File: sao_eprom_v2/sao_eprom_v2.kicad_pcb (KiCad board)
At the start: 4 copper layers, 62 parts, among them J1 Conn_01x03, J2 USB_C_Receptacle_USB2.0, J3 Conn_02x03_Odd_Even, Q1 RE1C002UNTCL, Q2 RE1C002ZPTL, Q3 RE1C002UNTCL, Q4 RE1C002ZPTL, Q5 RE1C002UNTCL, Q6 RE1C002ZPTL, U1 W25Q128JVS, U10 AP3012, U2 RP2040, U3 24LC00, U4 74HC273, U5 multi_eprom, U6 74LVC4245A-Q100, U7 74HC273, U8 SY8079AAC, U9 AP3012, X1 YSO110TR

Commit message: the experiment
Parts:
- added C14: 100n, Capacitor_SMD:C_0402_1005Metric_Pad0.74x0.62mm_HandSolder, F.Cu at (167.7, 90.5)
- added C15: 100n, Capacitor_SMD:C_0402_1005Metric_Pad0.74x0.62mm_HandSolder, F.Cu at (155.0, 85.0)
- added C16: 100n, Capacitor_SMD:C_0402_1005Metric_Pad0.74x0.62mm_HandSolder, F.Cu at (129.4, 69.5)
- added C17: 100n, Capacitor_SMD:C_0402_1005Metric_Pad0.74x0.62mm_HandSolder, F.Cu at (129.4, 71.8)
- added C18: 100n, Capacitor_SMD:C_0402_1005Metric_Pad0.74x0.62mm_HandSolder, F.Cu at (138.6, 64.5)
- added C19: 100n, Capacitor_SMD:C_0402_1005Metric_Pad0.74x0.62mm_HandSolder, F.Cu at (148.1, 71.6)
- added C20: 100n, Capacitor_SMD:C_0402_1005Metric_Pad0.74x0.62mm_HandSolder, F.Cu at (144.5, 71.6)
- added C21: 100n, Capacitor_SMD:C_0402_1005Metric_Pad0.74x0.62mm_HandSolder, F.Cu at (152.5, 63.0)
- added C22: 100n, Capacitor_SMD:C_0402_1005Metric_Pad0.74x0.62mm_HandSolder, F.Cu at (138.6, 65.5)
- C1, C2, C3, C4, C5, C6: footprint Capacitor_SMD:C_0402_1005Metric -> Capacitor_SMD:C_0402_1005Metric_Pad0.74x0.62mm_HandSolder
- C10, C11, C8, C9: footprint Capacitor_SMD:C_0603_1608Metric -> Capacitor_SMD:C_0603_1608Metric_Pad1.08x0.95mm_HandSolder
- C12, C13, C7: footprint Capacitor_SMD:C_0805_2012Metric -> Capacitor_SMD:C_0805_2012Metric_Pad1.18x1.45mm_HandSolder
- J3: value Conn_02x03_Odd_Even -> sao_v2_addon_tht; footprint Connector_PinHeader_2.54mm:PinHeader_2x03_P2.54mm_Vertical -> simple_add_on_v2:sao_v2_addon_tht
- U4, U7: value 74HC273 -> 74LS573
- moved U3 100.6 mm to (169.7, 94.0)
- moved U1 91.9 mm to (162.5, 83.0)
- moved R9 88.1 mm to (152.5, 66.0), turned to 180 degrees
- moved R8 87.9 mm to (152.5, 67.0), turned to 180 degrees
- moved C2 69.9 mm to (152.5, 65.0), turned to 180 degrees
- moved C4 69.9 mm to (152.5, 69.0), turned to 180 degrees
- moved C1 69.8 mm to (152.5, 64.0), turned to 180 degrees
- moved C3 69.8 mm to (152.5, 68.0), turned to 180 degrees
- moved U2 62.9 mm to (145.5, 64.2), turned to -90 degrees
- moved J3 53.3 mm to (109.8, 71.5)
- moved J2 37.9 mm to (106.0, 45.0), turned to -90 degrees
- moved C13 37.0 mm to (117.0, 41.5), turned to 90 degrees
- moved C12 33.5 mm to (115.0, 41.5), turned to 90 degrees
- moved C5 31.9 mm to (121.2, 40.7), turned to 90 degrees
- moved D4 31.8 mm to (118.5, 50.2), turned to 180 degrees
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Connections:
- net Net-(U2-VREG_VOUT) renamed +1V1
- net Net-(U5-D0) renamed /EPROM and level shifters/D0H
- net Net-(U5-D1) renamed /EPROM and level shifters/D1H
- net Net-(U5-D2) renamed /EPROM and level shifters/D2H
- net Net-(U5-D3) renamed /EPROM and level shifters/D3H
- net Net-(U5-D4) renamed /EPROM and level shifters/D4H
- net Net-(U5-D5) renamed /EPROM and level shifters/D5H
- net Net-(U5-D6) renamed /EPROM and level shifters/D6H
- net Net-(U5-D7) renamed /EPROM and level shifters/D7H
- C10 pad 2: +3.3V -> +3V3
- C8 pad 2: +3.3V -> +3V3
- D1 pad 1: /EPROM and level shifters/Vdet -> /EPROM and level shifters/Q15
- D2 pad 1: /EPROM and level shifters/VppA -> /EPROM and level shifters/VppB
- D2 pad 2: Net-(D2-A) -> /EPROM and level shifters/~{OE}
- D3 pad 1: /EPROM and level shifters/VppB -> /EPROM and level shifters/Q9
- D3 pad 2: /EPROM and level shifters/~{OE} -> Net-(D3-A)
- J2 pad B8: SBU1 -> SBU2
- J3 pad 1: GND -> +3V3
- J3 pad 2: +3V3 -> GND
- J3 pad 3: SCL -> SDA
- J3 pad 4: SDA -> SCL
- L2 pad 1: +3.3V -> +3V3
- L3 pad 1: +3.3V -> +3V3
- Q2 pad 3: /EPROM and level shifters/VppA -> /EPROM and level shifters/Q15
- Q6 pad 3: /EPROM and level shifters/Vdet -> /EPROM and level shifters/Q9
- U10 pad 5: +3.3V -> +3V3
- U2 pad 40: unconnected-(U2-GPIO28_ADC2-Pad40) -> SBU1
- U2 pad 41: unconnected-(U2-GPIO29_ADC3-Pad41) -> SBU2
- U4 pad 1: +3V3 -> GND
- U4 pad 12: Net-(U4-Q4) -> /EPROM and level shifters/Q7
- U4 pad 13: /EPROM and level shifters/A4 -> /EPROM and level shifters/Q6
- U4 pad 14: /EPROM and level shifters/A5 -> /EPROM and level shifters/Q5
- U4 pad 15: Net-(U4-Q5) -> /EPROM and level shifters/Q4
- U4 pad 16: Net-(U4-Q6) -> /EPROM and level shifters/Q3
- U4 pad 17: /EPROM and level shifters/A6 -> /EPROM and level shifters/Q2
- U4 pad 18: /EPROM and level shifters/A7 -> /EPROM and level shifters/Q1
- U4 pad 19: Net-(U4-Q7) -> /EPROM and level shifters/Q0
- U4 pad 2: Net-(U4-Q0) -> /EPROM and level shifters/A0
- U4 pad 3: /EPROM and level shifters/A0 -> /EPROM and level shifters/A1
- U4 pad 4: /EPROM and level shifters/A1 -> /EPROM and level shifters/A2
- U4 pad 5: Net-(U4-Q1) -> /EPROM and level shifters/A3
- U4 pad 6: Net-(U4-Q2) -> /EPROM and level shifters/A4
- U4 pad 7: /EPROM and level shifters/A2 -> /EPROM and level shifters/A5
- U4 pad 8: /EPROM and level shifters/A3 -> /EPROM and level shifters/A6
- U4 pad 9: Net-(U4-Q3) -> /EPROM and level shifters/A7
- U5 pad 1: /EPROM and level shifters/VppA -> /EPROM and level shifters/Q15
- U5 pad 10: Net-(U4-Q0) -> /EPROM and level shifters/Q0
- U5 pad 2: Net-(U5-A12) -> /EPROM and level shifters/Q12
- U5 pad 21: Net-(U5-A10) -> /EPROM and level shifters/Q10
- U5 pad 23: Net-(U5-A11) -> /EPROM and level shifters/Q11
- U5 pad 24: /EPROM and level shifters/Vdet -> /EPROM and level shifters/Q9
- U5 pad 25: Net-(U5-A8) -> /EPROM and level shifters/Q8
- U5 pad 26: Net-(U5-A13) -> /EPROM and level shifters/Q13
- U5 pad 27: Net-(U5-A14) -> /EPROM and level shifters/Q14
- U5 pad 3: Net-(U4-Q7) -> /EPROM and level shifters/Q7
- U5 pad 4: Net-(U4-Q6) -> /EPROM and level shifters/Q6
- U5 pad 5: Net-(U4-Q5) -> /EPROM and level shifters/Q5
- U5 pad 6: Net-(U4-Q4) -> /EPROM and level shifters/Q4
- U5 pad 7: Net-(U4-Q3) -> /EPROM and level shifters/Q3
- U5 pad 8: Net-(U4-Q2) -> /EPROM and level shifters/Q2
- U5 pad 9: Net-(U4-Q1) -> /EPROM and level shifters/Q1
- U7 pad 1: +3V3 -> GND
- U7 pad 12: Net-(U5-A12) -> Net-(D1-A)
- U7 pad 13: /EPROM and level shifters/A4 -> /EPROM and level shifters/Q14
- U7 pad 14: /EPROM and level shifters/A5 -> /EPROM and level shifters/Q13
- U7 pad 15: Net-(U5-A13) -> /EPROM and level shifters/Q12
- U7 pad 16: Net-(U5-A14) -> /EPROM and level shifters/Q11
- U7 pad 17: /EPROM and level shifters/A6 -> /EPROM and level shifters/Q10
- U7 pad 18: /EPROM and level shifters/A7 -> Net-(D3-A)
- U7 pad 19: Net-(D2-A) -> /EPROM and level shifters/Q8
- U7 pad 2: Net-(U5-A8) -> /EPROM and level shifters/A0
- U7 pad 3: /EPROM and level shifters/A0 -> /EPROM and level shifters/A1
- U7 pad 4: /EPROM and level shifters/A1 -> /EPROM and level shifters/A2
- U7 pad 5: Net-(D1-A) -> /EPROM and level shifters/A3
- U7 pad 6: Net-(U5-A10) -> /EPROM and level shifters/A4
- U7 pad 7: /EPROM and level shifters/A2 -> /EPROM and level shifters/A5
- U7 pad 8: /EPROM and level shifters/A3 -> /EPROM and level shifters/A6
- U7 pad 9: Net-(U5-A11) -> /EPROM and level shifters/A7
- U9 pad 5: +3.3V -> +3V3
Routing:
- net GND: track 0.00 -> 80.7 mm, vias 0 -> 16
- net +3V3: track 0.00 -> 60.9 mm, vias 0 -> 13
- net /EPROM and level shifters/VppB: track 0.00 -> 60.7 mm, vias 0 -> 2
- net /EPROM and level shifters/Q9: track 0.00 -> 58.6 mm, vias 0 -> 2
- net /EPROM and level shifters/D7H: track 0.00 -> 45.3 mm, vias 0 -> 2
- net /EPROM and level shifters/D3H: track 0.00 -> 44.7 mm, vias 0 -> 2
- net /EPROM and level shifters/D4H: track 0.00 -> 37.7 mm, vias 0 -> 2
- net /EPROM and level shifters/D6H: track 0.00 -> 37.7 mm, vias 0 -> 2
- net /EPROM and level shifters/Q10: track 0.00 -> 37.2 mm, vias 0 -> 1
- net /EPROM and level shifters/D5H: track 0.00 -> 33.4 mm, vias 0 -> 2
- net /EPROM and level shifters/Q11: track 0.00 -> 31.9 mm
- net Net-(D3-A): track 0.00 -> 28.1 mm
- net /EPROM and level shifters/A7: track 0.00 -> 27.5 mm, vias 0 -> 2
- net /EPROM and level shifters/Q8: track 0.00 -> 26.9 mm, vias 0 -> 1
- net /EPROM and level shifters/A6: track 0.00 -> 26.0 mm, vias 0 -> 2
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- added copper zone on F.Cu, net +1V1
- added copper zone on F.Cu, net +3V3

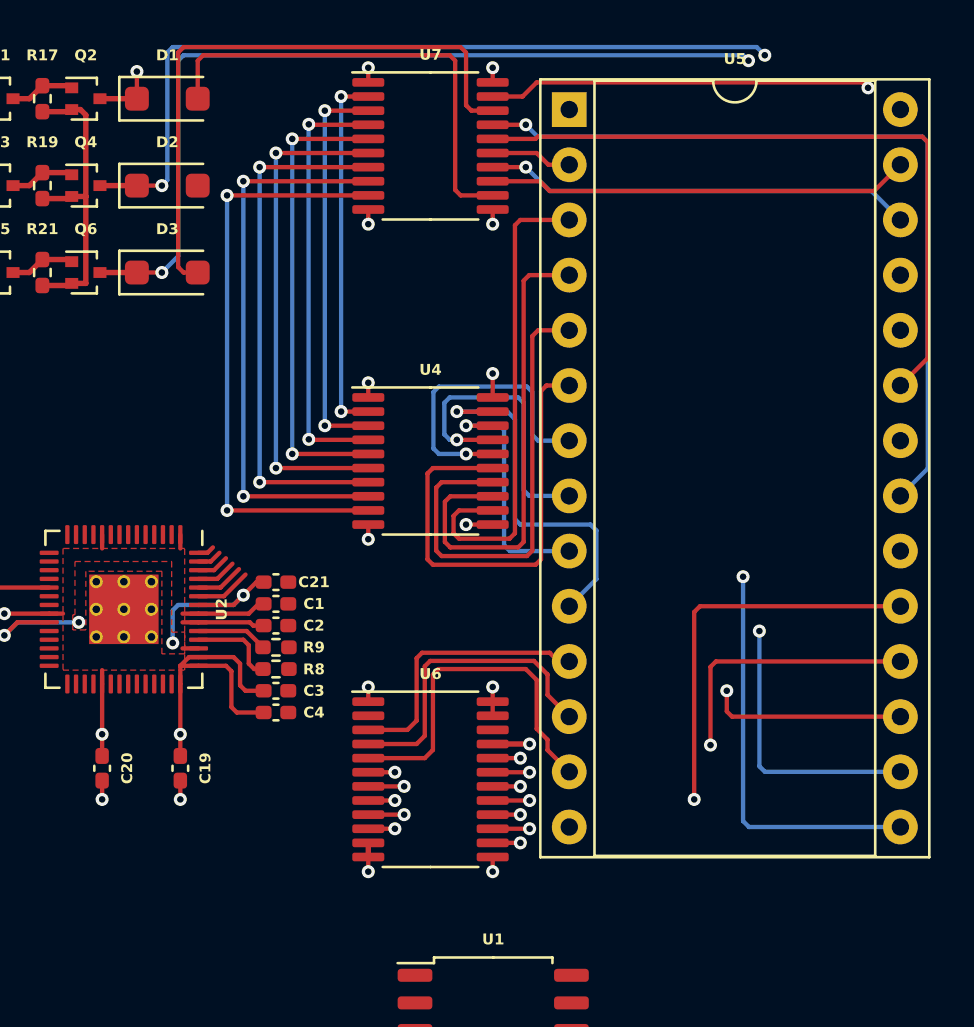
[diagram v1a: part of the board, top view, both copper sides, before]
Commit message: Flip the CHIPS upside down to make routing easier
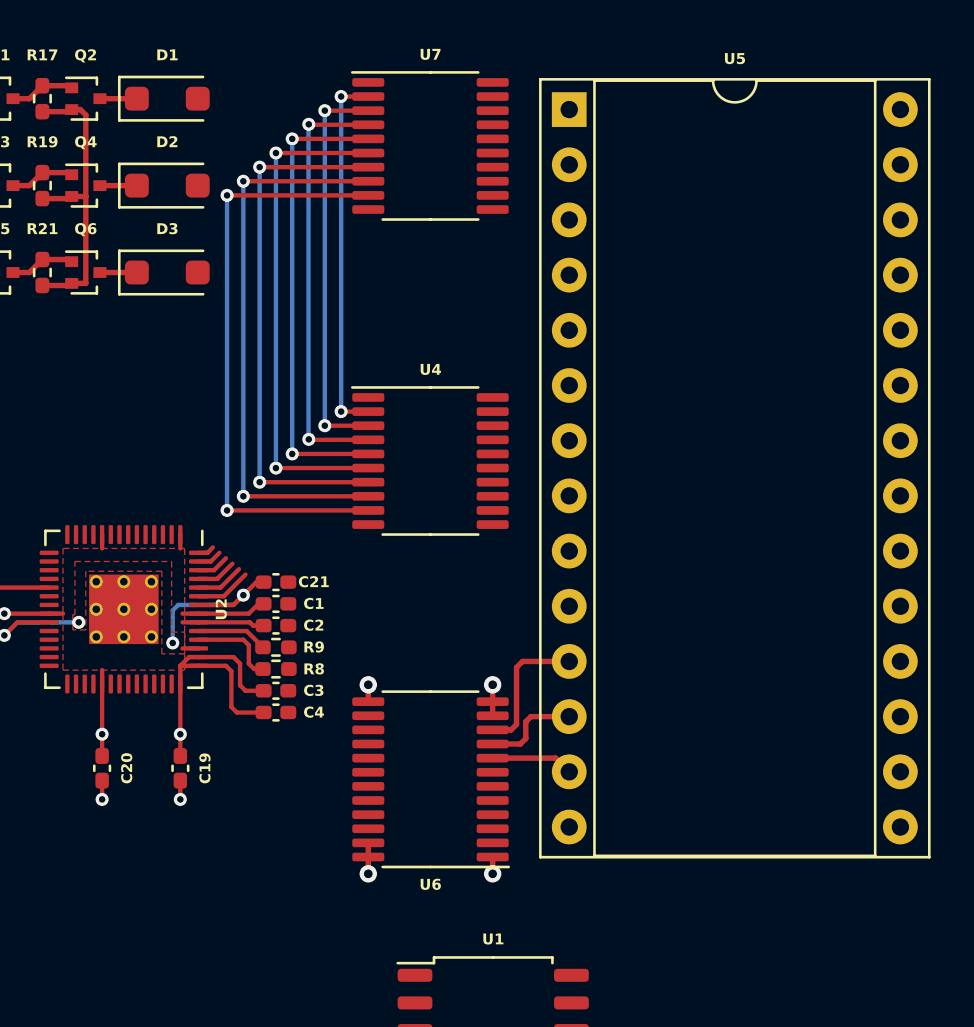
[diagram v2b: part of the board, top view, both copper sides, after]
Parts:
- turned U6 to 180 degrees
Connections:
- U4 pad 12: /EPROM and level shifters/Q7 -> /EPROM and level shifters/Q0
- U4 pad 13: /EPROM and level shifters/Q6 -> /EPROM and level shifters/Q1
- U4 pad 14: /EPROM and level shifters/Q5 -> /EPROM and level shifters/Q2
- U4 pad 15: /EPROM and level shifters/Q4 -> /EPROM and level shifters/Q3
- U4 pad 16: /EPROM and level shifters/Q3 -> /EPROM and level shifters/Q4
- U4 pad 17: /EPROM and level shifters/Q2 -> /EPROM and level shifters/Q5
- U4 pad 18: /EPROM and level shifters/Q1 -> /EPROM and level shifters/Q6
- U4 pad 19: /EPROM and level shifters/Q0 -> /EPROM and level shifters/Q7
- U4 pad 2: /EPROM and level shifters/A0 -> /EPROM and level shifters/A7
- U4 pad 3: /EPROM and level shifters/A1 -> /EPROM and level shifters/A6
- U4 pad 4: /EPROM and level shifters/A2 -> /EPROM and level shifters/A5
- U4 pad 5: /EPROM and level shifters/A3 -> /EPROM and level shifters/A4
- U4 pad 6: /EPROM and level shifters/A4 -> /EPROM and level shifters/A3
- U4 pad 7: /EPROM and level shifters/A5 -> /EPROM and level shifters/A2
- U4 pad 8: /EPROM and level shifters/A6 -> /EPROM and level shifters/A1
- U4 pad 9: /EPROM and level shifters/A7 -> /EPROM and level shifters/A0
- U6 pad 10: /EPROM and level shifters/D7H -> /EPROM and level shifters/D0H
- U6 pad 14: /EPROM and level shifters/D7 -> /EPROM and level shifters/D0
- U6 pad 15: /EPROM and level shifters/D6 -> /EPROM and level shifters/D1
- U6 pad 16: /EPROM and level shifters/D5 -> /EPROM and level shifters/D2
- U6 pad 17: /EPROM and level shifters/D4 -> /EPROM and level shifters/D3
- U6 pad 18: /EPROM and level shifters/D3 -> /EPROM and level shifters/D4
- U6 pad 19: /EPROM and level shifters/D2 -> /EPROM and level shifters/D5
- U6 pad 20: /EPROM and level shifters/D1 -> /EPROM and level shifters/D6
- U6 pad 21: /EPROM and level shifters/D0 -> /EPROM and level shifters/D7
- U6 pad 3: /EPROM and level shifters/D0H -> /EPROM and level shifters/D7H
- U6 pad 4: /EPROM and level shifters/D1H -> /EPROM and level shifters/D6H
- U6 pad 5: /EPROM and level shifters/D2H -> /EPROM and level shifters/D5H
- U6 pad 6: /EPROM and level shifters/D3H -> /EPROM and level shifters/D4H
- U6 pad 7: /EPROM and level shifters/D4H -> /EPROM and level shifters/D3H
- U6 pad 8: /EPROM and level shifters/D5H -> /EPROM and level shifters/D2H
- U6 pad 9: /EPROM and level shifters/D6H -> /EPROM and level shifters/D1H
- U7 pad 12: Net-(D1-A) -> /EPROM and level shifters/Q8
- U7 pad 13: /EPROM and level shifters/Q14 -> Net-(D3-A)
- U7 pad 14: /EPROM and level shifters/Q13 -> /EPROM and level shifters/Q10
- U7 pad 15: /EPROM and level shifters/Q12 -> /EPROM and level shifters/Q11
- U7 pad 16: /EPROM and level shifters/Q11 -> /EPROM and level shifters/Q12
- U7 pad 17: /EPROM and level shifters/Q10 -> /EPROM and level shifters/Q13
- U7 pad 18: Net-(D3-A) -> /EPROM and level shifters/Q14
- U7 pad 19: /EPROM and level shifters/Q8 -> Net-(D1-A)
- U7 pad 2: /EPROM and level shifters/A0 -> /EPROM and level shifters/A7
- U7 pad 3: /EPROM and level shifters/A1 -> /EPROM and level shifters/A6
- U7 pad 4: /EPROM and level shifters/A2 -> /EPROM and level shifters/A5
- U7 pad 5: /EPROM and level shifters/A3 -> /EPROM and level shifters/A4
- U7 pad 6: /EPROM and level shifters/A4 -> /EPROM and level shifters/A3
- U7 pad 7: /EPROM and level shifters/A5 -> /EPROM and level shifters/A2
- U7 pad 8: /EPROM and level shifters/A6 -> /EPROM and level shifters/A1
- U7 pad 9: /EPROM and level shifters/A7 -> /EPROM and level shifters/A0
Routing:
- net /EPROM and level shifters/VppB: track 60.7 -> 1.70 mm, vias 2 -> 0
- net /EPROM and level shifters/Q9: track 58.6 -> 1.70 mm, vias 2 -> 0
- net /EPROM and level shifters/D7H: track 45.3 -> 0.00 mm, vias 2 -> 0
- net /EPROM and level shifters/D3H: track 44.7 -> 0.00 mm, vias 2 -> 0
- net /EPROM and level shifters/D4H: track 37.7 -> 0.00 mm, vias 2 -> 0
- net /EPROM and level shifters/D6H: track 37.7 -> 0.00 mm, vias 2 -> 0
- net /EPROM and level shifters/Q10: track 37.2 -> 0.00 mm, vias 1 -> 0
- net /EPROM and level shifters/D5H: track 33.4 -> 0.00 mm, vias 2 -> 0
- net /EPROM and level shifters/Q11: track 31.9 -> 0.00 mm
- net Net-(D3-A): track 28.1 -> 0.00 mm
- net /EPROM and level shifters/Q8: track 26.9 -> 0.00 mm, vias 1 -> 0
- net /EPROM and level shifters/Q15: track 25.8 -> 1.70 mm, vias 1 -> 0
- net /EPROM and level shifters/Q7: track 22.5 -> 0.00 mm
- net /EPROM and level shifters/Q6: track 22.2 -> 0.00 mm
- net /EPROM and level shifters/Q5: track 21.9 -> 0.00 mm
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
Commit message: More tricky routing.
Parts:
- added C23: 100n, Capacitor_SMD:C_0402_1005Metric_Pad0.74x0.62mm_HandSolder, F.Cu at (149.0, 53.0)
- added H1: MountingHole_Pad, MountingHole:MountingHole_2.2mm_M2_Pad_Via, F.Cu at (97.2, 55.2)
- added H2: MountingHole_Pad, MountingHole:MountingHole_2.2mm_M2_Pad_Via, F.Cu at (97.2, 63.1)
- added H3: MountingHole_Pad, MountingHole:MountingHole_2.2mm_M2_Pad_Via, F.Cu at (180.5, 35.2)
- added H4: MountingHole_Pad, MountingHole:MountingHole_2.2mm_M2_Pad_Via, F.Cu at (180.5, 80.3)
- X1: value YSO110TR -> SX3M12.000M20F30TNN
- moved X1 66.5 mm to (146.0, 53.0), turned to 180 degrees
- moved C14 44.4 mm to (127.8, 71.0)
- moved U3 44.4 mm to (129.8, 74.5)
- moved C16 21.4 mm to (148.8, 60.4), turned to 180 degrees
- moved C17 20.4 mm to (148.8, 65.2), turned to 180 degrees
- moved U1 18.4 mm to (145.6, 75.6), turned to 180 degrees
- moved C15 17.3 mm to (139.4, 77.5), turned to 180 degrees
- moved C19 15.8 mm to (134.4, 63.7), turned to 0 degrees
- moved C4 15.5 mm to (137.0, 68.1), turned to 90 degrees
- moved C20 15.3 mm to (134.4, 60.1), turned to 0 degrees
- moved C3 14.5 mm to (138.0, 68.1), turned to 90 degrees
- moved R8 13.5 mm to (139.0, 68.1), turned to 90 degrees
- moved R9 12.7 mm to (140.0, 68.1), turned to 90 degrees
- moved C2 11.9 mm to (141.0, 68.1), turned to 90 degrees
- moved C22 11.4 mm to (140.6, 54.2), turned to -90 degrees
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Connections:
- net Net-(J2-D+-PadA6) renamed USB_D+
- net Net-(J2-D--PadA7) renamed USB_D-
- net Net-(U1-CLK) renamed /QSPI_CLK
- net Net-(U1-DI(IO0)) renamed /QSPI_D0
- net Net-(U1-DO(IO1)) renamed /QSPI_D1
- net Net-(U1-IO2) renamed /QSPI_D2
- net Net-(U1-IO3) renamed /QSPI_D3
- net Net-(U1-~{CS}) renamed /~{QSPI_CS}
- net USB_DM renamed /RP2040_D-
- net USB_DP renamed /RP2040_D+
- U2 pad 11: /EPROM and level shifters/D0 -> /EPROM and level shifters/A0
- U2 pad 12: /EPROM and level shifters/D1 -> /EPROM and level shifters/A1
- U2 pad 13: /EPROM and level shifters/D2 -> /EPROM and level shifters/A2
- U2 pad 14: /EPROM and level shifters/D3 -> /EPROM and level shifters/A3
- U2 pad 15: /EPROM and level shifters/D4 -> /EPROM and level shifters/A4
- U2 pad 16: /EPROM and level shifters/D5 -> /EPROM and level shifters/A5
- U2 pad 17: /EPROM and level shifters/D6 -> /EPROM and level shifters/A6
- U2 pad 18: /EPROM and level shifters/D7 -> /EPROM and level shifters/A7
- U2 pad 2: /EPROM and level shifters/A0 -> /EPROM and level shifters/D0
- U2 pad 3: /EPROM and level shifters/A1 -> /EPROM and level shifters/D1
- U2 pad 4: /EPROM and level shifters/A2 -> /EPROM and level shifters/D2
- U2 pad 5: /EPROM and level shifters/A3 -> /EPROM and level shifters/D3
- U2 pad 6: /EPROM and level shifters/A4 -> /EPROM and level shifters/D4
- U2 pad 7: /EPROM and level shifters/A5 -> /EPROM and level shifters/D5
- U2 pad 8: /EPROM and level shifters/A6 -> /EPROM and level shifters/D6
- U2 pad 9: /EPROM and level shifters/A7 -> /EPROM and level shifters/D7
- U6 pad 10: /EPROM and level shifters/D0H -> /EPROM and level shifters/D7H
- U6 pad 14: /EPROM and level shifters/D0 -> /EPROM and level shifters/D7
- U6 pad 15: /EPROM and level shifters/D1 -> /EPROM and level shifters/D6
- U6 pad 16: /EPROM and level shifters/D2 -> /EPROM and level shifters/D5
- U6 pad 17: /EPROM and level shifters/D3 -> /EPROM and level shifters/D4
- U6 pad 18: /EPROM and level shifters/D4 -> /EPROM and level shifters/D3
- U6 pad 19: /EPROM and level shifters/D5 -> /EPROM and level shifters/D2
- U6 pad 20: /EPROM and level shifters/D6 -> /EPROM and level shifters/D1
- U6 pad 21: /EPROM and level shifters/D7 -> /EPROM and level shifters/D0
- U6 pad 3: /EPROM and level shifters/D7H -> /EPROM and level shifters/D0H
- U6 pad 4: /EPROM and level shifters/D6H -> /EPROM and level shifters/D1H
- U6 pad 5: /EPROM and level shifters/D5H -> /EPROM and level shifters/D2H
- U6 pad 6: /EPROM and level shifters/D4H -> /EPROM and level shifters/D3H
- U6 pad 7: /EPROM and level shifters/D3H -> /EPROM and level shifters/D4H
- U6 pad 8: /EPROM and level shifters/D2H -> /EPROM and level shifters/D5H
- U6 pad 9: /EPROM and level shifters/D1H -> /EPROM and level shifters/D6H
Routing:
- net /EPROM and level shifters/D7H: track 0.00 -> 23.3 mm
- net /EPROM and level shifters/D3H: track 0.00 -> 22.1 mm
- net /EPROM and level shifters/D6H: track 0.00 -> 21.4 mm
- net /EPROM and level shifters/D2: track 0.00 -> 21.0 mm
- net /EPROM and level shifters/D0: track 0.00 -> 21.0 mm
- net /EPROM and level shifters/D1: track 0.00 -> 20.8 mm
- net /~{QSPI_CS}: track 0.77 -> 21.5 mm
- net /EPROM and level shifters/D3: track 0.00 -> 20.4 mm
- net /QSPI_D1: track 1.13 -> 21.4 mm
- net /EPROM and level shifters/D4: track 0.00 -> 20.2 mm
- net /EPROM and level shifters/D5: track 0.00 -> 20.0 mm
- net /QSPI_D2: track 1.49 -> 21.3 mm
- net /EPROM and level shifters/D6: track 0.00 -> 19.8 mm
- net /EPROM and level shifters/D4H: track 0.00 -> 19.8 mm
- net /EPROM and level shifters/D7: track 0.00 -> 19.6 mm
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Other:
- board text added: "Length tuned"
